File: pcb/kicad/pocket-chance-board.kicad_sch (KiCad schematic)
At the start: 0 parts

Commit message: PCB phase 3: schematic generator and first full schematic (ERC 0 errors); JST-only battery with reverse-polarity guard; project library tables; ignore KiCad lock files
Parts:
- added BT2: CR1220, Battery:BatteryHolder_Keystone_3001_1x12mm, symbol Device:Battery_Cell
- added C1, C10, C18, C19, C2, C24, C27, C28, C3, C34, C35, C36, C37, C39, C4, C5, C6, C7, C8, C9: 100nF, Capacitor_SMD:C_0402_1005Metric, symbol Device:C
- added C11, C21, C22, C23, C25, C26, C32, C33, C38: 10uF, Capacitor_SMD:C_0603_1608Metric, symbol Device:C
- added C12: 2.2uF, Capacitor_SMD:C_0603_1608Metric, symbol Device:C
- added C13, C14, C15: 4.7uF, Capacitor_SMD:C_0402_1005Metric, symbol Device:C
- added C16, C17: 15pF, Capacitor_SMD:C_0402_1005Metric, symbol Device:C
- added C20, C30, C31: 1uF, Capacitor_SMD:C_0603_1608Metric, symbol Device:C
- added C29: 10nF, Capacitor_SMD:C_0402_1005Metric, symbol Device:C
- added D1: CHG, LED_SMD:LED_0603_1608Metric, symbol Device:LED
- added D2: USER, LED_SMD:LED_0603_1608Metric, symbol Device:LED
- added J1: SWD, Connector_PinHeader_1.27mm:PinHeader_2x05_P1.27mm_Vertical_SMD, symbol Connector:Conn_ARM_JTAG_SWD_10
- added J2: USB4085-GF-A, Connector_USB:USB_C_Receptacle_GCT_USB4085, symbol Connector:USB_C_Receptacle_USB2.0_16P
- added J3: LiPo JST-PH 2.0mm (+ pin 1), Connector_JST:JST_PH_S2B-PH-SM4-TB_1x02-1MP_P2.00mm_Horizontal, symbol Connector:Conn_01x02_Socket
- added J4: LCD 1.54in ST7789 module, Connector_PinSocket_2.54mm:PinSocket_1x08_P2.54mm_Vertical_SMD_Pin1Left, symbol Connector:Conn_01x08_Socket
- added J5: Speaker JST-PH, Connector_JST:JST_PH_S2B-PH-SM4-TB_1x02-1MP_P2.00mm_Horizontal, symbol Connector:Conn_01x02_Socket
- added J6: microSD Molex 104031-0811, Connector_Card:microSD_HC_Molex_104031-0811, symbol Connector:Micro_SD_Card
- added J7: STEMMA QT, Connector_JST:JST_SH_SM04B-SRSS-TB_1x04-1MP_P1.00mm_Horizontal, symbol Connector:Conn_01x04_Socket
- added J8: Expansion, Connector_PinHeader_2.54mm:PinHeader_1x06_P2.54mm_Vertical, symbol Connector:Conn_01x06_Pin
- added JP2: RTC INT to GP14, Jumper:SolderJumper-2_P1.3mm_Open_Pad1.0x1.5mm, symbol Jumper:SolderJumper_2_Open
- added L1: 3.3uH AOTA-B201610S3R3-101-T, Inductor_SMD:L_0805_2012Metric, symbol Device:L
- added L2: 2.2uH, Inductor_SMD:L_1210_3225Metric, symbol Device:L
- added Q1: FS8205A, Package_SO:TSSOP-8_4.4x3mm_P0.65mm, symbol pcb_custom:FS8205A
- added Q2: DMG2305UX, Package_TO_SOT_SMD:SOT-23, symbol Transistor_FET:AO3401A
- added R1: 200R, Resistor_SMD:R_0402_1005Metric, symbol Device:R
- added R10, R11: 27R, Resistor_SMD:R_0402_1005Metric, symbol Device:R
- added R12, R13, R26, R27, R28, R29, R30, R34, R37, R4, R6, R7: 10k, Resistor_SMD:R_0402_1005Metric, symbol Device:R
- added R14: 1.8k, Resistor_SMD:R_0402_1005Metric, symbol Device:R
- added R15: 3.0k, Resistor_SMD:R_0402_1005Metric, symbol Device:R
- added R16: 47k, Resistor_SMD:R_0402_1005Metric, symbol Device:R
- added R17: 1.5k, Resistor_SMD:R_0402_1005Metric, symbol Device:R
- added R18, R21, R25, R3, R35, R5: 1k, Resistor_SMD:R_0402_1005Metric, symbol Device:R
- added R19, R23, R24: 100k, Resistor_SMD:R_0402_1005Metric, symbol Device:R
- added R2: 33R, Resistor_SMD:R_0402_1005Metric, symbol Device:R
- added R20: 100R, Resistor_SMD:R_0402_1005Metric, symbol Device:R
- added R22: 0R, Resistor_SMD:R_0603_1608Metric, symbol Device:R
- added R31, R32: 4.7k, Resistor_SMD:R_0402_1005Metric, symbol Device:R
- added R33: 470R, Resistor_SMD:R_0402_1005Metric, symbol Device:R
- added R36: 5.6k, Resistor_SMD:R_0402_1005Metric, symbol Device:R
- added R8, R9: 5.1k, Resistor_SMD:R_0402_1005Metric, symbol Device:R
- added SW1: BOOT, Button_Switch_SMD:SW_SPST_PTS645Sx43SMTR92, symbol Switch:SW_Push
- added SW10: JOY LEFT, pcb_custom:Alps_SKRHABE010, symbol Switch:SW_Push
- added SW11: JOY RIGHT, pcb_custom:Alps_SKRHABE010, symbol Switch:SW_Push
- added SW12: JOY PRESS, pcb_custom:Alps_SKRHABE010, symbol Switch:SW_Push
- added SW2: RESET, Button_Switch_SMD:SW_SPST_PTS645Sx43SMTR92, symbol Switch:SW_Push
- added SW3: POWER PCM12, Button_Switch_SMD:SW_SPDT_PCM12, symbol Switch:SW_SPDT
- added SW4: A, Button_Switch_SMD:SW_SPST_PTS645Sx43SMTR92, symbol Switch:SW_Push
- added SW5: B, Button_Switch_SMD:SW_SPST_PTS645Sx43SMTR92, symbol Switch:SW_Push
- added SW6: X, Button_Switch_SMD:SW_SPST_PTS645Sx43SMTR92, symbol Switch:SW_Push
- added SW7: Y, Button_Switch_SMD:SW_SPST_PTS645Sx43SMTR92, symbol Switch:SW_Push
- added SW8: JOY UP, pcb_custom:Alps_SKRHABE010, symbol Switch:SW_Push
- added SW9: JOY DOWN, pcb_custom:Alps_SKRHABE010, symbol Switch:SW_Push
- added TP1: VBUS, TestPoint:TestPoint_Pad_D1.5mm, symbol Connector:TestPoint
- added TP2: VSYS, TestPoint:TestPoint_Pad_D1.5mm, symbol Connector:TestPoint
- added TP3: +3V3, TestPoint:TestPoint_Pad_D1.5mm, symbol Connector:TestPoint
- added TP4: 1V1, TestPoint:TestPoint_Pad_D1.5mm, symbol Connector:TestPoint
- added TP5, TP6: GND, TestPoint:TestPoint_Pad_D1.5mm, symbol Connector:TestPoint
- added TP7: BAT+, TestPoint:TestPoint_Pad_D1.5mm, symbol Connector:TestPoint
- added TP8: RUN, TestPoint:TestPoint_Pad_D1.5mm, symbol Connector:TestPoint
- added U1: RP2350A, Package_DFN_QFN:QFN-60-1EP_7x7mm_P0.4mm_EP3.4x3.4mm, symbol MCU_RaspberryPi:RP2350A
- added U10: LSM6DSOXTR, pcb_custom:ST_LGA-14_2.5x3mm, symbol Sensor_Motion:LSM6DSM
- added U11: RM2, pcb_custom:RM2, symbol pcb_custom:RM2
- added U2: W25Q128JVSIQ, Package_SO:SOIC-8_5.3x5.3mm_P1.27mm, symbol Memory_Flash:W25Q128JVS
- added U3: APS6404L-3SQR-SN, Package_SO:SOIC-8_3.9x4.9mm_P1.27mm, symbol Memory_RAM:APS6404L-3SQRx-SN
- added U4: USBLC6-2SC6, Package_TO_SOT_SMD:SOT-23-6, symbol Power_Protection:USBLC6-2SC6
- added U5: BQ24074RGTR, Package_DFN_QFN:VQFN-16-1EP_3x3mm_P0.5mm_EP1.6x1.6mm, symbol Battery_Management:BQ24074RGT
- added U6: TPS63001DRCR, Package_SON:Texas_DRC0010J_ThermalVias, symbol Regulator_Switching:TPS63001
- added U7: DW01A, Package_TO_SOT_SMD:SOT-23-6, symbol Battery_Management:DW01A
- added U8: PAM8302AASCR, Package_SO:SOIC-8_3.9x4.9mm_P1.27mm, symbol Amplifier_Audio:PAM8302AAS
- added U9: DS3231MZ+, Package_SO:SOIC-8_3.9x4.9mm_P1.27mm, symbol Timer_RTC:DS3231MZ
- added Y1: 12MHz ABM8-272-T3, Crystal:Crystal_SMD_3225-4Pin_3.2x2.5mm, symbol Device:Crystal_GND24
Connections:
- new net +3V3: C1.1, C11.1, C13.1, C18.1, C19.1, C2.1, C25.1, C26.1, C3.1, C32.1, C33.1, C34.1, C35.1, C36.1, C37.1, C38.1, C39.1, C4.1, C5.1, C6.1, C7.1, J1.1 (VTref), J4.1 (Pin_1), J6.4 (VDD), J7.2 (Pin_2), J8.1 (Pin_1), R1.1, R2.1, R26.1, R27.1, R28.1, R29.1, R30.1, R31.1, R32.1, R4.1, R6.1, R7.1, TP3.1, U1.1 (IOVDD), U1.11 (IOVDD), U1.20 (IOVDD), U1.30 (IOVDD), U1.38 (IOVDD), U1.45 (IOVDD), U1.49 (VREG_VIN), U1.53 (USB_OTP_VDD), U1.54 (QSPI_IOVDD), U10.12 (CS), U10.5 (VDDIO), U10.8 (VDD), U11.14 (VDDIO), U11.16 (VIN), U2.8 (VCC), U3.8 (VDD), U6.1 (VOUT), U6.10 (FB), U8.1 (~{SD}), U8.6 (VDD), U9.2 (VCC)
- new net 1V1: C10.1, C14.1, C8.1, C9.1, L1.2, TP4.1, U1.23 (DVDD), U1.39 (DVDD), U1.50 (VREG_FB), U1.6 (DVDD)
- new net ADC_AVDD: C12.1, R1.2, U1.44 (ADC_AVDD)
- new net AUDIO_FILT: C29.1, C30.1, R25.2
- new net AUDIO_INN: C31.2, U8.4 (IN-)
- new net AUDIO_INP: C30.2, U8.3 (IN+)
- new net AUDIO_PWM: R25.1, U1.34 (GPIO22)
- new net BAT+: C22.1, R20.1, R22.2, R23.1, TP7.1, U5.2 (BAT), U5.3 (BAT)
- new net BAT-: C27.2, J3.2 (Pin_2), Q1.1 (S1), Q2.1 (G), U7.6 (GND)
- new net BB_L1: L2.1, U6.4 (L1)
- new net BB_L2: L2.2, U6.2 (L2)
- new net BOOT_SW: R5.2, SW1.1
- new net BTN_A: SW4.1, U1.19 (GPIO15)
- new net BTN_B: SW5.1, U1.28 (GPIO17)
- new net BTN_X: SW6.1, U1.31 (GPIO19)
- new net BTN_Y: SW7.1, U1.33 (GPIO21)
- new net CC1: J2.A5 (CC1), R8.1
- new net CC2: J2.B5 (CC2), R9.1
- new net CELL_G: Q2.3 (D), R22.1
- new net CELL_P: J3.1 (Pin_1), Q2.2 (S)
- new net CHG_EN1: R13.2, U5.6 (EN1)
- new net CHG_LED: D1.2 (A), R18.2
- new net CHG_STAT: D1.1 (K), U5.9 (~{CHG})
- new net EXP_GP1: J8.5 (Pin_5), U1.3 (GPIO1)
- new net FET_D: Q1.5 (D2), Q1.6 (D2), Q1.7 (D1), Q1.8 (D1)
- new net GND: BT2.2 (-), C1.2, C10.2, C11.2, C12.2, C13.2, C14.2, C15.2, C16.2, C17.2, C18.2, C19.2, C2.2, C20.2, C21.2, C22.2, C23.2, C24.2, C25.2, C26.2, C28.2, C29.2, C3.2, C31.1, C32.2, C33.2, C34.2, C35.2, C36.2, C37.2, C38.2, C39.2, C4.2, C5.2, C6.2, C7.2, C8.2, C9.2, D2.1 (K), J1.3 (GND), J1.5 (GND), J1.9 (GNDDetect), J2.A1 (GND), J2.A12 (GND), J2.B1 (GND), J2.B12 (GND), J2.SH (SHIELD), J4.2 (Pin_2), J6.6 (VSS), J6.SH (SHIELD), J7.1 (Pin_1), J8.2 (Pin_2), Q1.3 (S2), R12.2, R14.2, R15.2, R16.2, R17.2, R19.2, R21.2, R24.2, R37.2, R8.2, R9.2, SW1.2, SW10.2, SW11.2, SW12.2, SW2.2, SW3.3 (C), SW4.2, SW5.2, SW6.2, SW7.2, SW8.2, SW9.2, TP5.1, TP6.1, U1.47 (VREG_PGND), U1.61 (GND), U10.1 (SDO/SA0), U10.6 (GND), U10.7 (GND), U11.1 (GND), U11.11 (GND), U11.15 (GND), U11.21 (GND), U11.4 (GND), U11.7 (GND), U2.4 (GND), U3.4 (VSS), U4.2 (GND), U5.17 (VSS), U5.4 (~{CE}), U5.5 (EN2), U5.8 (VSS), U6.11 (PGND), U6.3 (PGND), U6.7 (PS/SYNC), U6.9 (GND), U8.7 (GND), U9.5 (GND), Y1.2 (G), Y1.4 (G)
- new net ILIM: R15.1, U5.12 (ILIM)
- new net IMU_INT: JP2.2 (B), U1.18 (GPIO14), U10.4 (INT1)
- new net ISET: R14.1, U5.16 (ISET)
- new net ITERM: R17.1, U5.15 (ITERM)
- new net JOY_DOWN: SW9.1, U1.29 (GPIO18)
- new net JOY_LEFT: SW10.1, U1.27 (GPIO16)
- new net JOY_PRESS: SW12.1, U1.5 (GPIO3)
- new net JOY_RIGHT: SW11.1, U1.32 (GPIO20)
- new net JOY_UP: SW8.1, U1.4 (GPIO2)
- new net LCD_BL: J4.8 (Pin_8), U1.17 (GPIO13)
- new net LCD_CS: J4.5 (Pin_5), U1.13 (GPIO9)
- new net LCD_DC: J4.6 (Pin_6), U1.12 (GPIO8)
- new net LCD_MOSI: J4.3 (Pin_3), U1.15 (GPIO11)
- new net LCD_RST: J4.7 (Pin_7), U1.16 (GPIO12)
- new net LCD_SCK: J4.4 (Pin_4), U1.14 (GPIO10)
- new net LED_A: D2.2 (A), R35.2
- new net PROT_CS: R21.1, U7.2 (CS)
- new net PROT_OC: Q1.4 (G2), U7.3 (OC)
- new net PROT_OD: Q1.2 (G1), U7.1 (OD)
- new net PROT_VCC: C27.1, R20.2, U7.5 (VCC)
- new net PSRAM_CS: R6.2, U1.2 (GPIO0), U3.1 (~{CE})
- new net PWR_EN: R19.1, SW3.2 (B), U6.6 (EN)
- new net QSPI_SCLK: U1.56 (QSPI_SCLK), U2.6 (CLK), U3.6 (SCLK)
- new net QSPI_SD0: U1.57 (QSPI_SD0), U2.5 (DI/IO_{0}), U3.5 (SI/SIO0)
- new net QSPI_SD1: U1.59 (QSPI_SD1), U2.2 (DO/IO_{1}), U3.2 (SO/SIO1)
- new net QSPI_SD2: U1.58 (QSPI_SD2), U2.3 (~{WP}/IO_{2}), U3.3 (SIO2)
- new net QSPI_SD3: U1.55 (QSPI_SD3), U2.7 (~{HOLD}/~{RESET}/IO_{3}), U3.7 (SIO3)
- new net QSPI_SS: R4.2, R5.1, U1.60 (~{QSPI_SS}), U2.1 (~{CS})
- new net RTC_INT: JP2.1 (A), U9.3 (~{INT}/SQW)
- new net RTC_VBAT: BT2.1 (+), U9.6 (VBAT)
- new net RUN: J1.10 (~{RESET}), R7.2, SW2.1, TP8.1, U1.26 (RUN)
- new net SCL: J7.4 (Pin_4), J8.4 (Pin_4), R32.2, U1.41 (GPIO27/ADC1), U10.13 (SCL), U9.8 (SCL)
- new net SDA: J7.3 (Pin_3), J8.3 (Pin_3), R31.2, U1.40 (GPIO26/ADC0), U10.14 (SDA), U9.7 (SDA)
- new net SD_CS: J6.2 (DAT3/CD), R27.2, U1.8 (GPIO5)
- new net SD_DAT1: J6.8 (DAT1), R30.2
- new net SD_DAT2: J6.1 (DAT2), R26.2
- new net SD_MISO: J6.7 (DAT0), R29.2, U1.7 (GPIO4)
- new net SD_MOSI: J6.3 (CMD), R28.2, U1.10 (GPIO7)
- new net SD_SCK: J6.5 (CLK), U1.9 (GPIO6)
- new net SPK+: J5.1 (Pin_1), U8.5 (OUT+)
- new net SPK-: J5.2 (Pin_2), U8.8 (OUT-)
- new net SWCLK: J1.4 (SWCLK/TCK), U1.24 (SWCLK)
- new net SWDIO: J1.2 (SWDIO/TMS), U1.25 (SWDIO)
- new net TMR: R16.1, U5.14 (TMR)
- new net TS: R12.1, U5.1 (TS)
- new net USB_DM: J2.A7 (D-), J2.B7 (D-), R11.1, U4.3 (I/O2), U4.4 (I/O2)
- new net USB_DM_R: R11.2, U1.51 (USB_DM)
- new net USB_DP: J2.A6 (D+), J2.B6 (D+), R10.1, U4.1 (I/O1), U4.6 (I/O1)
- new net USB_DP_R: R10.2, U1.52 (USB_DP)
- new net VBAT_SENSE: C28.1, J8.6 (Pin_6), R23.2, R24.1, U1.42 (GPIO28/ADC2)
- new net VBUS: C20.1, J2.A4 (VBUS), J2.A9 (VBUS), J2.B4 (VBUS), J2.B9 (VBUS), R13.1, R36.1, TP1.1, U4.5 (VBUS), U5.13 (IN)
- new net VREG_AVDD: C15.1, R2.2, U1.46 (VREG_AVDD)
- new net VREG_LX: L1.1, U1.48 (VREG_LX)
- new net VSYS: C21.1, C23.1, C24.1, R18.1, SW3.1 (A), TP2.1, U5.10 (OUT), U5.11 (OUT), U6.5 (VIN), U6.8 (VINA)
- new net WL_CLK: U1.43 (GPIO29/ADC3), U11.3 (SCLK)
- new net WL_CS: U1.37 (GPIO25), U11.9 (CS)
- new net WL_DATA: R33.2, R34.2, U1.36 (GPIO24), U11.5 (DATA_IN)
- new net WL_DOUT: R33.1, U11.6 (DATA_OUT)
- new net WL_GPIO0: R35.1, U11.8 (WL_GPIO0)
- new net WL_IRQ: R34.1, U11.10 (nIRQ)
- new net WL_REG_ON: U1.35 (GPIO23), U11.12 (WL_ON), U11.13 (BT_ON)
- new net WL_VBUS_SENSE: R36.2, R37.1, U11.17 (WL_GPIO2)
- new net XIN: C16.1, U1.21 (XIN), Y1.1
- new net XOUT: R3.1, U1.22 (XOUT)
- new net XOUT_X: C17.1, R3.2, Y1.3
- no-connect marks 0 -> 19
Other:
- company: (none) -> Pocket Chance

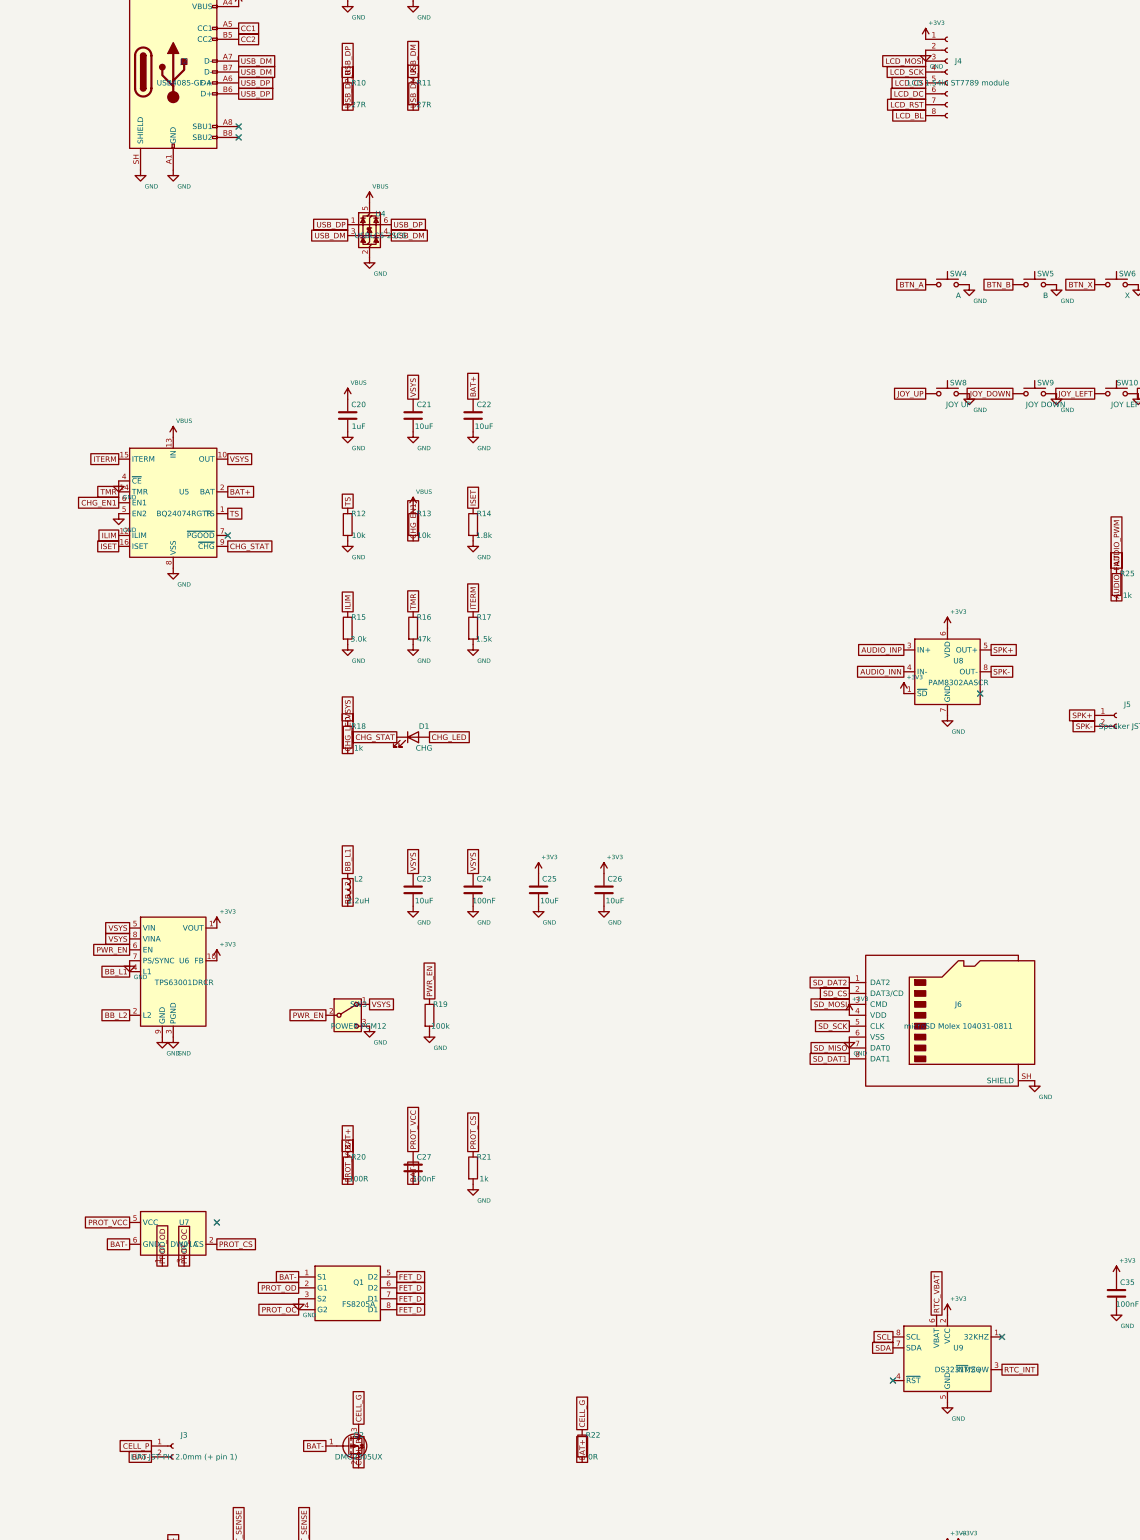
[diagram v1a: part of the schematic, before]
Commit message: Screen socket is JST-PH 8-pin (module has a PH2.0 cable); REVIEW-1 against the RP2350 design guide
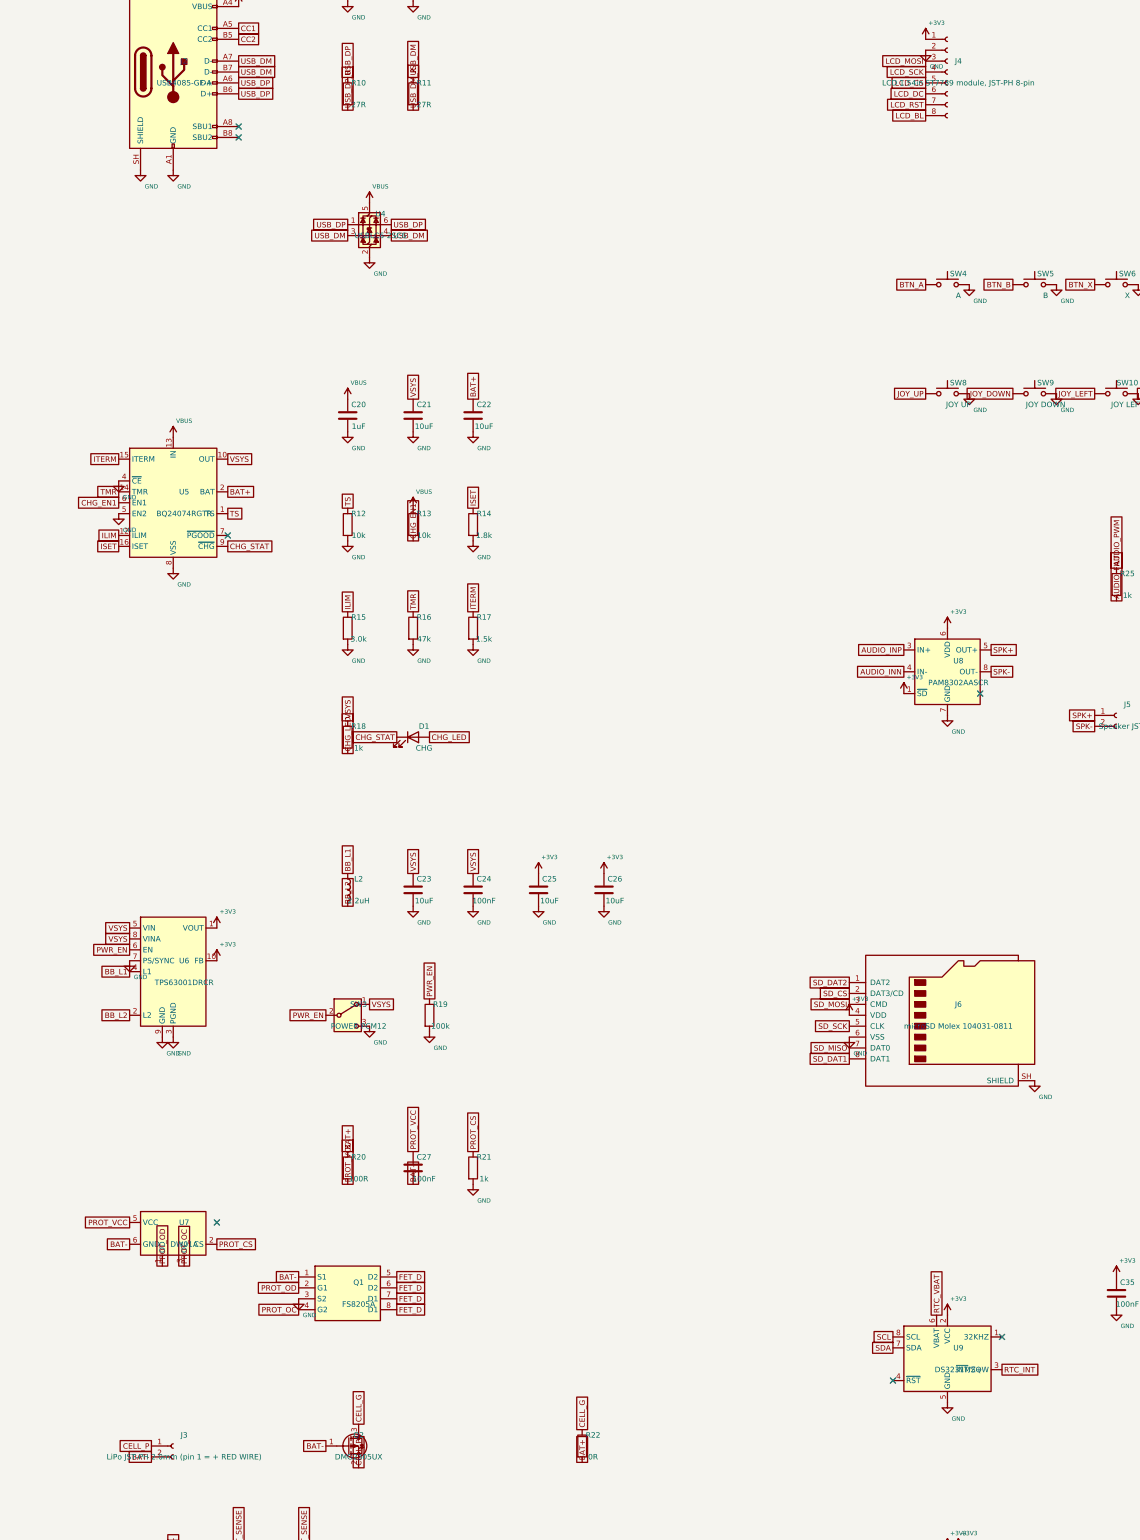
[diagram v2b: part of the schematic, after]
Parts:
- J3: value LiPo JST-PH 2.0mm (+ pin 1) -> LiPo JST-PH 2.0mm (pin 1 = + RED WIRE)
- J4: value LCD 1.54in ST7789 module -> LCD 1.54in ST7789 module, JST-PH 8-pin; footprint Connector_PinSocket_2.54mm:PinSocket_1x08_P2.54mm_Vertical_SMD_Pin1Left -> Connector_JST:JST_PH_S8B-PH-SM4-TB_1x08-1MP_P2.00mm_Horizontal
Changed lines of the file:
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@@
 			)
 		)
-		(property "Value" "LiPo JST-PH 2.0mm (+ pin 1)"
+		(property "Value" "LiPo JST-PH 2.0mm (pin 1 = + RED WIRE)"
 			(at 302.26 402.59 0)
 			(effects
@@
 			)
 		)
-		(property "Value" "LCD 1.54in ST7789 module"
+		(property "Value" "LCD 1.54in ST7789 module, JST-PH 8-pin"
 			(at 482.6 82.55 0)
 			(effects
@@
 			)
 		)
-		(property "Footprint" "Connector_PinSocket_2.54mm:PinSocket_1x08_P2.54mm_Vertical_SMD_Pin1Left"
+		(property "Footprint" "Connector_JST:JST_PH_S8B-PH-SM4-TB_1x08-1MP_P2.00mm_Horizontal"
 			(at 480.06 80.01 0)
 			(effects
